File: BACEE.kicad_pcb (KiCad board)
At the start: 2 copper layers, 42.7 x 24.4 mm, 20 parts, among them J2 I2C connector, J3 Digital pins, J4 Serial connector, J5 ICSP, U1 24LC1025, U2 DS1337S+, U3 24LC1025, U4 ATMEGA328P-AU, Y1 32768KHz, Y2 16MHz

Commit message: Created new netlist file.
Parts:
- added J1: GND_rail, Connector_PinHeader_2.54mm:PinHeader_1x05_P2.54mm_Vertical, F.Cu at (147.9, 97.8)
- added J10: Conn_01x01_Female, Connector_Pin:Pin_D1.0mm_L10.0mm_LooseFit, F.Cu at (162.0, 97.7)
- added J11: Conn_01x01_Female, Connector_Pin:Pin_D1.0mm_L10.0mm_LooseFit, F.Cu at (158.5, 104.6)
- added J12: Conn_01x01_Female, Connector_Pin:Pin_D1.0mm_L10.0mm_LooseFit, F.Cu at (162.0, 101.2)
- added J13: Conn_01x01_Female, Connector_Pin:Pin_D1.0mm_L10.0mm_LooseFit, F.Cu at (155.1, 108.1)
- added J14: Conn_01x01_Female, Connector_Pin:Pin_D1.0mm_L10.0mm_LooseFit, F.Cu at (165.4, 97.7)
- added J15: Conn_01x01_Female, Connector_Pin:Pin_D1.0mm_L10.0mm_LooseFit, F.Cu at (155.1, 97.7)
- added J16: Conn_01x01_Female, Connector_Pin:Pin_D1.0mm_L10.0mm_LooseFit, F.Cu at (162.0, 104.6)
- added J17: Conn_01x01_Female, Connector_Pin:Pin_D1.0mm_L10.0mm_LooseFit, F.Cu at (165.4, 101.2)
- added J18: Conn_01x01_Female, Connector_Pin:Pin_D1.0mm_L10.0mm_LooseFit, F.Cu at (168.9, 97.7)
- added J19: Conn_01x01_Female, Connector_Pin:Pin_D1.0mm_L10.0mm_LooseFit, F.Cu at (162.0, 108.1)
- added J20: Conn_01x01_Female, Connector_Pin:Pin_D1.0mm_L10.0mm_LooseFit, F.Cu at (165.4, 104.6)
- added J21: Conn_01x01_Female, Connector_Pin:Pin_D1.0mm_L10.0mm_LooseFit, F.Cu at (168.9, 101.2)
- added J22: Conn_01x01_Female, Connector_Pin:Pin_D1.0mm_L10.0mm_LooseFit, F.Cu at (165.4, 108.1)
- added J23: Conn_01x01_Female, Connector_Pin:Pin_D1.0mm_L10.0mm_LooseFit, F.Cu at (168.9, 104.6)
- added J24: Conn_01x01_Female, Connector_Pin:Pin_D1.0mm_L10.0mm_LooseFit, F.Cu at (168.9, 108.1)
- added J25: Conn_01x01_Female, Connector_Pin:Pin_D1.0mm_L10.0mm_LooseFit, F.Cu at (158.5, 108.1)
- added J26: Conn_01x01_Female, Connector_Pin:Pin_D1.0mm_L10.0mm_LooseFit, F.Cu at (158.5, 97.7)
- added J6: 5V_Rail, Connector_PinHeader_2.54mm:PinHeader_1x05_P2.54mm_Vertical, F.Cu at (151.5, 97.8)
- added J7: Conn_01x01_Female, Connector_Pin:Pin_D1.0mm_L10.0mm_LooseFit, F.Cu at (155.1, 101.2)
- added J8: Conn_01x01_Female, Connector_Pin:Pin_D1.0mm_L10.0mm_LooseFit, F.Cu at (158.5, 101.2)
- added J9: Conn_01x01_Female, Connector_Pin:Pin_D1.0mm_L10.0mm_LooseFit, F.Cu at (155.1, 104.6)
- J5: value ICSP -> ICSP connector
- Y1: value 32768KHz -> Crystal32768KHz
- Y2: value 16MHz -> Crystal 16MHz

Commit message: Completed design of extended board.
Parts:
- moved J6 16.5 mm to (142.7, 111.8), turned to 90 degrees
- moved J11 13.7 mm to (144.8, 104.6)
- moved J14 13.7 mm to (151.7, 97.7)
- moved J17 13.7 mm to (151.7, 101.2)
- moved J18 13.7 mm to (155.2, 97.7)
- moved J20 13.7 mm to (151.7, 104.6)
- moved J21 13.7 mm to (155.2, 101.2)
- moved J22 13.7 mm to (151.7, 108.1)
- moved J23 13.7 mm to (155.2, 104.6)
- moved J24 13.7 mm to (155.2, 108.1)
- moved J25 13.7 mm to (144.8, 108.1)
- moved J26 13.7 mm to (144.8, 97.7)
- moved J8 13.7 mm to (144.8, 101.2)
- moved J10 13.7 mm to (148.3, 97.7)
- moved J12 13.7 mm to (148.3, 101.2)
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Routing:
- net GND: track 176.9 -> 198.3 mm
- net /Vcc: track 127.4 -> 146.7 mm
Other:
- board size 42.7 x 24.4 mm -> 63 x 24.4 mm
- board text added: "5V"

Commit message: Adjusted designators, units etc as per Larry's feedback.
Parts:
- J5: value ICSP connector -> ICSP
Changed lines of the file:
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@@
       (effects (font (size 0.6 0.6) (thickness 0.15)))
     )
-    (fp_text value "ICSP connector" (at 1.27 7.41) (layer F.SilkS)
+    (fp_text value ICSP (at 1.27 7.41) (layer F.SilkS)
       (effects (font (size 0.8 0.8) (thickness 0.15)))
     )

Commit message: Corrected a value, added 3D renders.
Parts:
- Y1: value Crystal32768KHz -> Crystal 32768 kHz
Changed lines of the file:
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@@
     (34 B.Paste user hide)
     (35 F.Paste user hide)
-    (36 B.SilkS user)
+    (36 B.SilkS user hide)
     (37 F.SilkS user)
     (38 B.Mask user)
@@
       (effects (font (size 0.6 0.6) (thickness 0.15)))
     )
-    (fp_text value Crystal32768KHz (at 0 1.95) (layer F.SilkS)
+    (fp_text value "Crystal 32768 kHz" (at 0 1.95) (layer F.SilkS)
       (effects (font (size 0.6 0.6) (thickness 0.1)))
     )

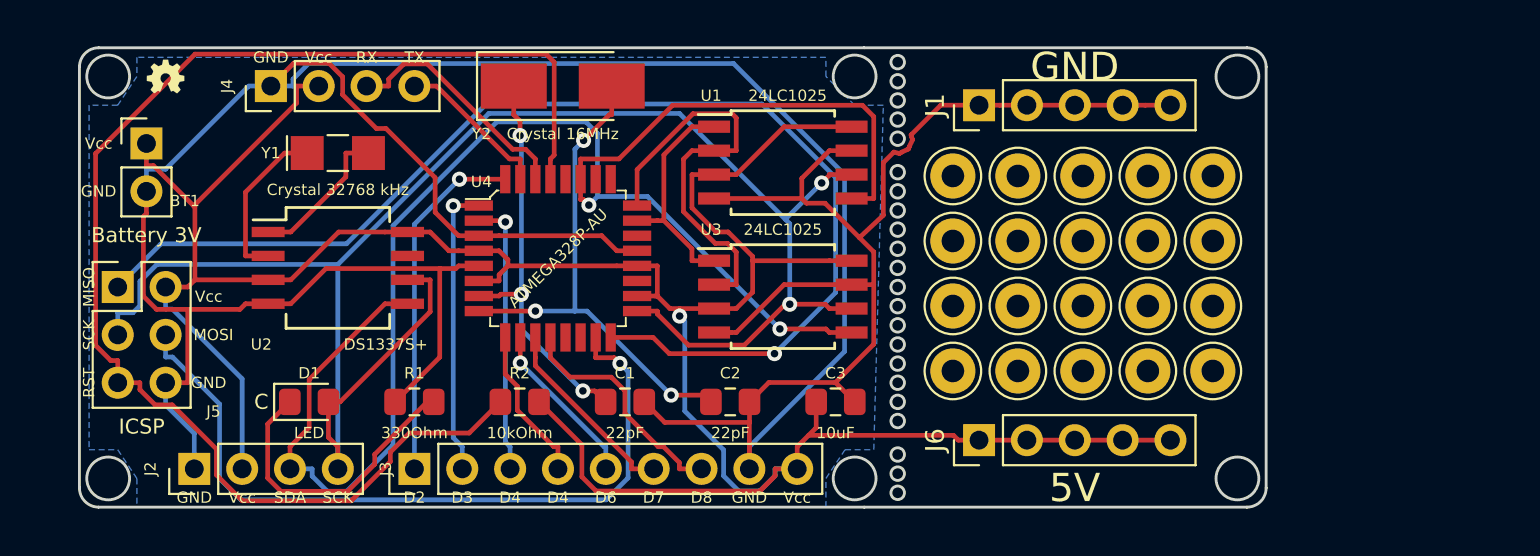
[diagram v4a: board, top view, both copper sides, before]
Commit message: Fixed error in EEPROM addressing pins.
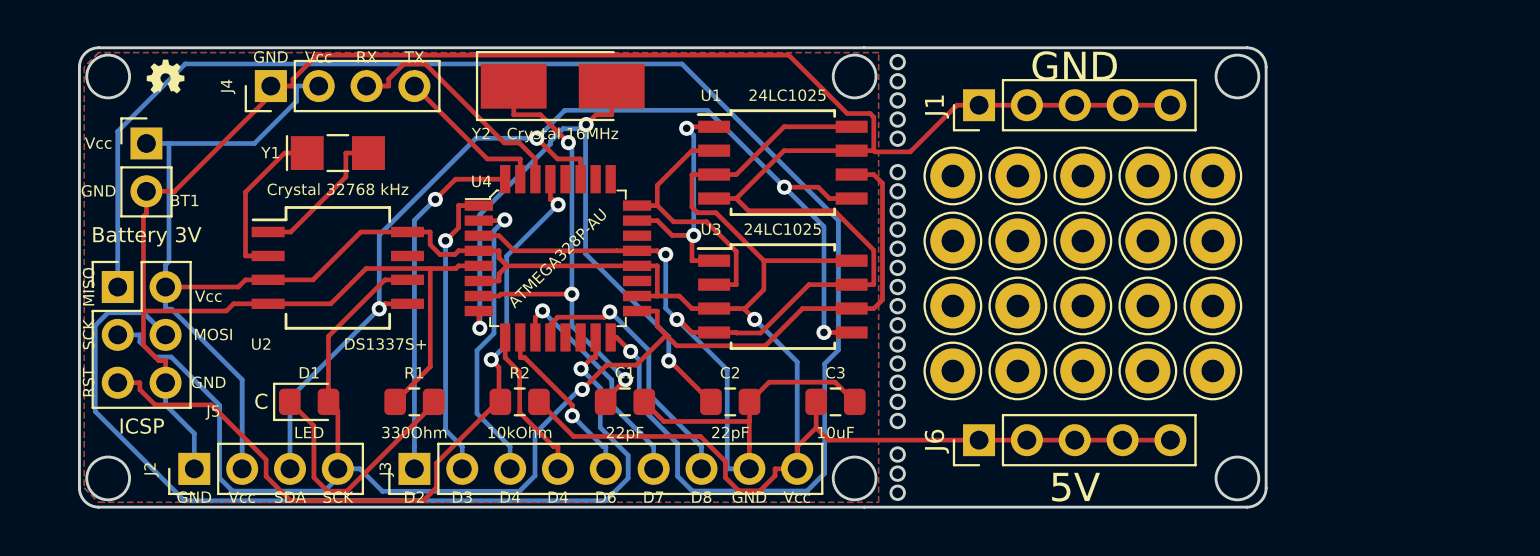
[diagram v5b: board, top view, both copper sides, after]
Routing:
- net /RESET: track 72.3 -> 40.3 mm, vias 0 -> 2
- net /SDA: track 90.0 -> 59.6 mm, vias 2 -> 4
- net GND: track 198.3 -> 176.9 mm, vias 0 -> 2
- net /MISO: track 63.5 -> 82.7 mm
- net /SCK: track 91.3 -> 77.2 mm, vias 2 -> 1
- net /ADDS2: track 22.6 -> 14.1 mm
- net /MOSI: track 40.4 -> 48.8 mm
- net Net-(C2-Pad1): track 27.1 -> 35.2 mm
- net /Vcc: track 146.7 -> 142.0 mm
- net Net-(C1-Pad1): track 21.5 -> 25.5 mm
- net Net-(D1-Pad1): track 15.9 -> 13.2 mm
- net /D7: track 10.3 -> 12.4 mm, vias 0 -> 1
- net /D8: track 12.4 -> 14.5 mm, vias 0 -> 1
- net /D4: track 14.6 -> 15.9 mm
- net /ADDS1: track 12.1 -> 13.2 mm, vias 0 -> 2
- added copper zone on F.Cu, net /Vcc
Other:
- board text added: "Arduino clone with - 2Mbit EEPROM - Clock & calendar - I2C, SPI & GPIOs Version 1.1 - Prototyping"
- board text removed: "Arduino clone with - 2Mbit EEPROM - Clock & calendar - I2C, SPI & GPIOs"
